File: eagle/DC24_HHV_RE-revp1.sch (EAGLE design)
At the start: 11 parts, among them U1 PIC12F1571

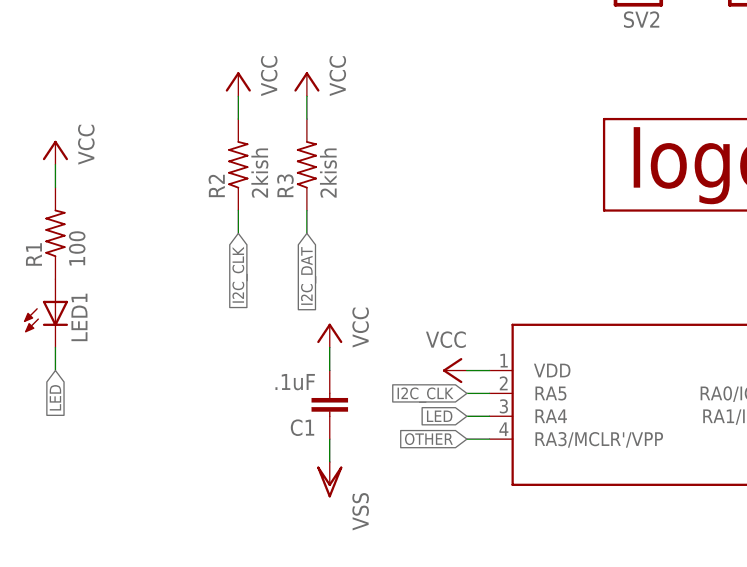
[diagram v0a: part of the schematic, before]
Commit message: Added note on schematic about running a short between I2C clk and dat in Rev A
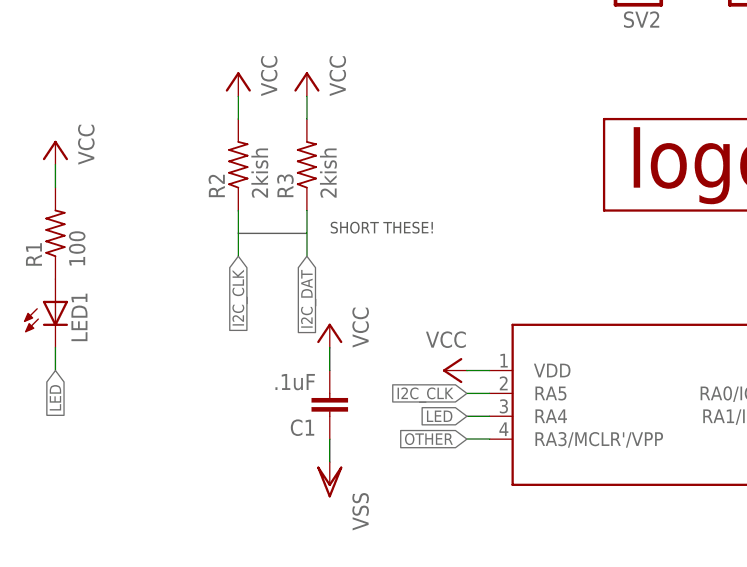
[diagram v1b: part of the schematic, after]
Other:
- note added: "SHORT THESE!"
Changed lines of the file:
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@@
 <?xml version="1.0" encoding="utf-8"?>
 <!DOCTYPE eagle SYSTEM "eagle.dtd">
-<eagle version="6.6.0">
+<eagle version="6.5.0">
 <drawing>
 <settings>
@@
 <sheet>
 <plain>
+<wire x1="-66.04" y1="55.88" x2="-58.42" y2="55.88" width="0.1524" layer="97"/>
+<text x="-55.88" y="55.88" size="1.27" layer="97">SHORT THESE!</text>
 </plain>
 <instances>
@@
 <segment>
 <pinref part="R3" gate="G$1" pin="1"/>
-<wire x1="-58.42" y1="58.42" x2="-58.42" y2="55.88" width="0.1524" layer="91"/>
-<label x="-58.42" y="55.88" size="1.27" layer="95" rot="R270" xref="yes"/>
+<wire x1="-58.42" y1="58.42" x2="-58.42" y2="53.34" width="0.1524" layer="91"/>
+<label x="-58.42" y="53.34" size="1.27" layer="95" rot="R270" xref="yes"/>
 </segment>
 <segment>
@@
 <segment>
 <pinref part="R2" gate="G$1" pin="1"/>
-<wire x1="-66.04" y1="58.42" x2="-66.04" y2="55.88" width="0.1524" layer="91"/>
-<label x="-66.04" y="55.88" size="1.27" layer="95" rot="R270" xref="yes"/>
-</segment>
-<segment>
+<wire x1="-66.04" y1="58.42" x2="-66.04" y2="53.34" width="0.1524" layer="91"/>
+<label x="-66.04" y="53.34" size="1.27" layer="95" rot="R270" xref="yes"/>
+</segment>
+<segment>

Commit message: Added note to schematic about handling jumper pad in Rev A
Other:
- note added: "Set up to have a clever hidden short. Don't want epoxy on there after all. HHV tools could be mis-used."
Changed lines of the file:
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@@
 <wire x1="-66.04" y1="55.88" x2="-58.42" y2="55.88" width="0.1524" layer="97"/>
 <text x="-55.88" y="55.88" size="1.27" layer="97">SHORT THESE!</text>
+<text x="12.7" y="22.86" size="1.27" layer="97">Set up to have a clever hidden
+short. Don't want epoxy on
+there after all. HHV tools
+could be mis-used.</text>
 </plain>
 <instances>
@@
 </schematic>
 </drawing>
+<compatibility>
+<note version="6.3" minversion="6.2.2" severity="warning">
+Since Version 6.2.2 text objects can contain more than one line,
+which will not be processed correctly with this version.
+</note>
+</compatibility>
 </eagle>
